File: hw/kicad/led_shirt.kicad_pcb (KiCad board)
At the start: 2 copper layers, 47.5 x 19.8 mm, 26 parts, among them J1 10103593-0001LF, J2 2_PIN_HDR, J3 2_PIN_HDR, J4 5_PIN_HDR, Q1 PN_MOSFET_DUAL, SW1 SW_PUSH, U1 AP3012, U2 PIC12F1822, U3 MCP73831

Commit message: save gerbers and new renders
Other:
- board size 47.5 x 19.8 mm -> 36.8 x 19.8 mm
- board text added: "BAT+"
- board text added: "BAT-"
- board text added: "LED+"
- board text added: "LED-"
- board text added: "github.com/noahp/ledshirt v3.0"
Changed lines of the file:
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@@
-(kicad_pcb (version 4) (host pcbnew 4.0.0-rc2-stable)
+(kicad_pcb (version 4) (host pcbnew 4.0.0-rc1-stable)
   (general
     (links 67)
     (no_connects 0)
-    (area 111.061499 77.279499 158.940501 97.472501)
+    (area 115.34578 76.46528 153.703721 98.16672)
     (thickness 1.6002)
-    (drawings 20)
+    (drawings 13)
     (tracks 231)
     (zones 0)
@@
     (visible_elements 7FFFFF3F)
     (pcbplotparams
-      (layerselection 0x00030_80000001)
+      (layerselection 0x010f0_80000001)
       (usegerberextensions true)
       (excludeedgelayer true)
@@
   (module kicadlib:SMD_0603_R placed (layer Front)
     (at 144.018 87.376 180)
-    (fp_text reference R3 (at -2.794 1.27 180) (layer F.SilkS)
+    (fp_text reference R3 (at -2.413 -1.397 180) (layer F.SilkS)
       (effects (font (size 0.75 0.75) (thickness 0.12)))
     )
@@
   (module kicadlib:SMD_0603_R placed (layer Front)
     (at 144.78 80.772 270)
-    (fp_text reference R5 (at -0.762 1.27 270) (layer F.SilkS)
+    (fp_text reference R5 (at -2.286 -1.524 360) (layer F.SilkS)
       (effects (font (size 0.75 0.75) (thickness 0.12)))
     )
@@
   (module kicadlib:SMD_SOIC-8 placed (layer Front)
     (at 145.542 90.424 270)
-    (fp_text reference U2 (at -1.778 0.254 360) (layer F.SilkS)
+    (fp_text reference U2 (at 0.762 5.334 360) (layer F.SilkS)
       (effects (font (size 0.75 0.75) (thickness 0.12)))
     )
@@
   (module kicadlib:SMD_IND_6.8x6.8_SRR6038-100Y placed (layer Front)
     (at 131.826 82.804)
-    (fp_text reference L1 (at 0 -2.286) (layer F.SilkS)
+    (fp_text reference L1 (at -4.318 2.286) (layer F.SilkS)
       (effects (font (size 0.75 0.75) (thickness 0.12)))
     )
@@
   (module kicadlib:SMD_SOT23-5 placed (layer Front)
     (at 125.222 82.804 270)
-    (fp_text reference U1 (at 2.54 2.286 360) (layer F.SilkS)
+    (fp_text reference U1 (at -1.524 1.397 360) (layer F.SilkS)
       (effects (font (size 0.75 0.75) (thickness 0.12)))
     )
@@
   (module kicadlib:TH_JST_2PIN_RIGHTANGLE (layer Front)
     (at 121.158 80.518 270)
-    (fp_text reference J2 (at 1.4 -2.2 360) (layer F.SilkS)
+    (fp_text reference J2 (at 4.953 2.794 360) (layer F.SilkS)
       (effects (font (size 0.75 0.75) (thickness 0.12)))
     )
@@
   (module kicadlib:spst_pushbutton_smd placed (layer Front)
     (at 147.828 95.25 90)
-    (fp_text reference SW1 (at 9.906 2.286 180) (layer F.SilkS)
+    (fp_text reference SW1 (at 9.398 2.286 180) (layer F.SilkS)
       (effects (font (size 0.75 0.75) (thickness 0.12)))
     )
@@
     )
   )
-  (gr_line (start 116.586 90.424) (end 116.586 96.012) (angle 90) (layer Edge.Cuts) (width 0.381))
-  (gr_line (start 116.586 78.74) (end 116.586 84.328) (angle 90) (layer Edge.Cuts) (width 0.381))
-  (gr_line (start 153.416 90.424) (end 153.416 96.012) (angle 90) (layer Edge.Cuts) (width 0.381))
-  (gr_line (start 153.416 78.74) (end 153.416 84.328) (angle 90) (layer Edge.Cuts) (width 0.381))
-  (gr_circle (center 114.3 87.376) (end 114.3 85.852) (layer Edge.Cuts) (width 0.381))
-  (gr_arc (start 114.3 87.376) (end 114.3 90.424) (angle 90) (layer Edge.Cuts) (width 0.381))
-  (gr_arc (start 114.3 87.376) (end 111.252 87.376) (angle 90) (layer Edge.Cuts) (width 0.381))
-  (gr_line (start 114.3 90.424) (end 116.586 90.424) (angle 90) (layer Edge.Cuts) (width 0.381))
-  (gr_line (start 114.3 84.328) (end 116.586 84.328) (angle 90) (layer Edge.Cuts) (width 0.381))
+  (gr_text BAT- (at 121.158 84.455) (layer B.SilkS)
+    (effects (font (size 1 1) (thickness 0.15)) (justify mirror))
+  )
+  (gr_text BAT+ (at 121.158 78.74) (layer B.SilkS)
+    (effects (font (size 1 1) (thickness 0.15)) (justify mirror))
+  )
+  (gr_text LED- (at 148.209 78.74) (layer B.SilkS)
+    (effects (font (size 1 1) (thickness 0.15)) (justify mirror))
+  )
+  (gr_text LED+ (at 148.209 84.455) (layer B.SilkS)
+    (effects (font (size 1 1) (thickness 0.15)) (justify mirror))
+  )
+  (gr_text "github.com/noahp/ledshirt\nv3.0" (at 133.604 82.804) (layer B.Mask)
+    (effects (font (size 1 1) (thickness 0.15)) (justify mirror))
+  )
+  (gr_line (start 153.416 78.74) (end 153.416 96.012) (angle 90) (layer Edge.Cuts) (width 0.381))
+  (gr_line (start 116.586 78.74) (end 116.586 96.012) (angle 90) (layer Edge.Cuts) (width 0.381))
   (gr_line (start 117.856 97.282) (end 152.146 97.282) (angle 90) (layer Edge.Cuts) (width 0.381))
-  (gr_line (start 155.702 90.424) (end 153.416 90.424) (angle 90) (layer Edge.Cuts) (width 0.381))
-  (gr_line (start 155.702 84.328) (end 153.416 84.328) (angle 90) (layer Edge.Cuts) (width 0.381))
-  (gr_arc (start 155.702 87.376) (end 158.75 87.376) (angle 90) (layer Edge.Cuts) (width 0.381))
-  (gr_arc (start 155.702 87.376) (end 155.702 84.328) (angle 90) (layer Edge.Cuts) (width 0.381))
-  (gr_circle (center 155.702 87.376) (end 155.702 88.9) (layer Edge.Cuts) (width 0.381))
   (gr_line (start 152.146 77.47) (end 117.856 77.47) (angle 90) (layer Edge.Cuts) (width 0.381))
   (gr_arc (start 117.856 96.012) (end 117.856 97.282) (angle 90) (layer Edge.Cuts) (width 0.381))

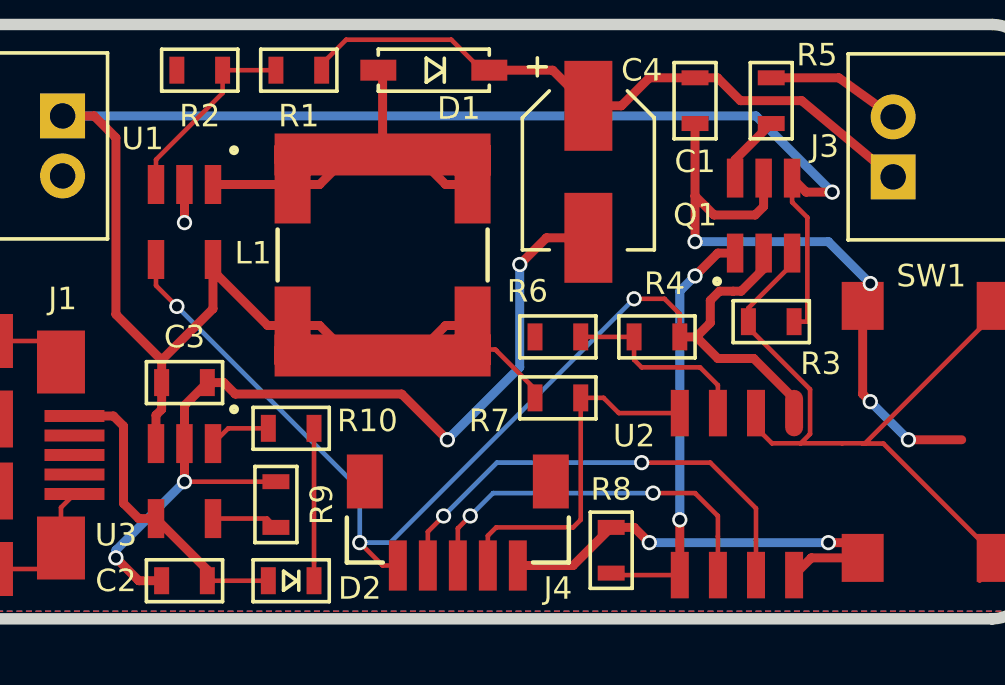
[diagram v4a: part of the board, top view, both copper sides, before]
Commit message: add add pull-down to lps net, to prevent p-fet leakage from enabling 12v boost when lps is disabled
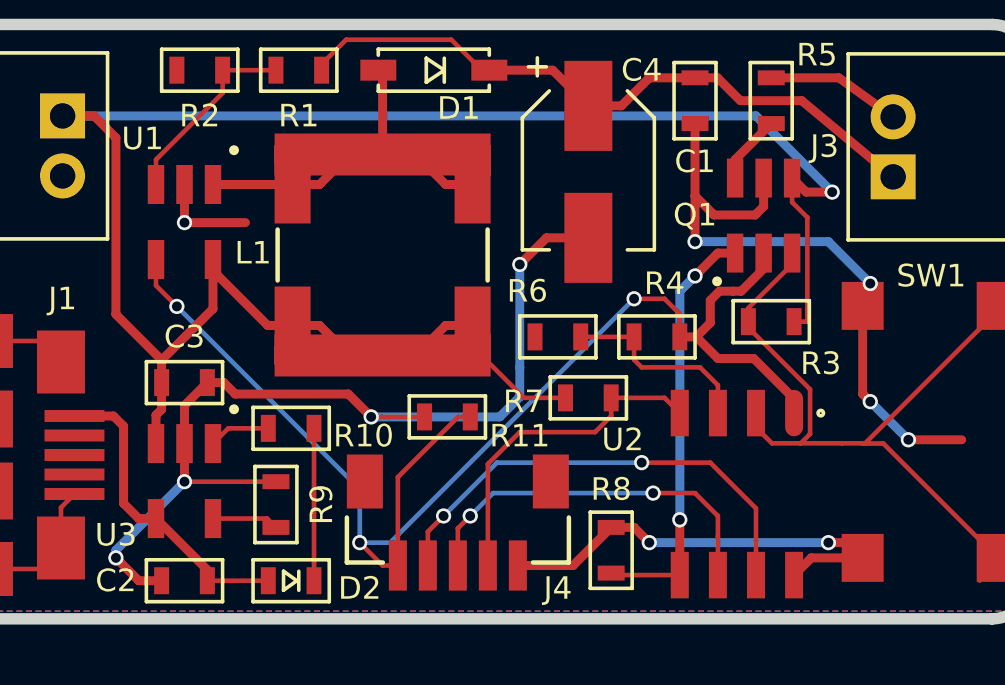
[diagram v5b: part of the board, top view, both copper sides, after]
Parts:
- added R11: 10K, kicadlib:SMD_0603_R, F.Cu at (133.2, 90.6)
- R1: value 10kΩ -> 82kΩ
- moved R7 1.02 mm to (137.9, 89.9)
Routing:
- net /lps: track 38.1 -> 44.3 mm
- net GND: track 76.2 -> 80.0 mm
- net /vbat: track 67.3 -> 68.3 mm
- net /mclr: track 11.9 -> 11.3 mm
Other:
- board text added: "github.com/noahp/ledshirt v3.1"
- board text removed: "github.com/noahp/ledshirt v3.0"
